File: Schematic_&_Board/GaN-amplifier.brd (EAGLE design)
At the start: 120.7 x 50.8 mm, 80 parts, among them IC1 LT3080, J1 JOHNSON_SMA_EDGE_LAUNCH_142-0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, J2 JOHNSON_SMA_EDGE_LAUNCH_142-0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, Q1 MMBT3906LT1SMD, T1 IRL3714S, T2 IRL3714S, T3 IRL3714S, T4 IRL3714S, T5 BSP89, U1 TPS7A30XX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

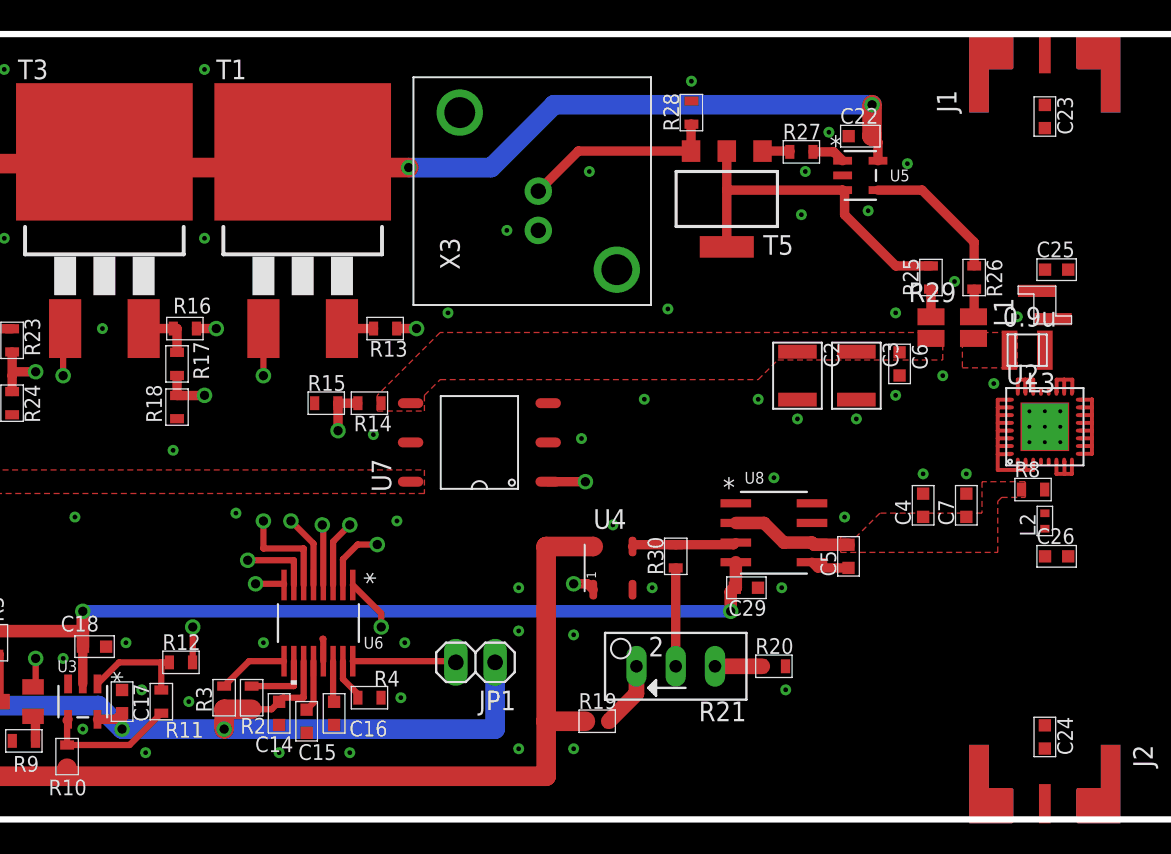
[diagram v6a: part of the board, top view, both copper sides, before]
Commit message: Finished Layout, Starting BOM
I've finished the layout up to getting final RF trace widths set (per
manufacturer specs) and started compiling a BOM.

DSB
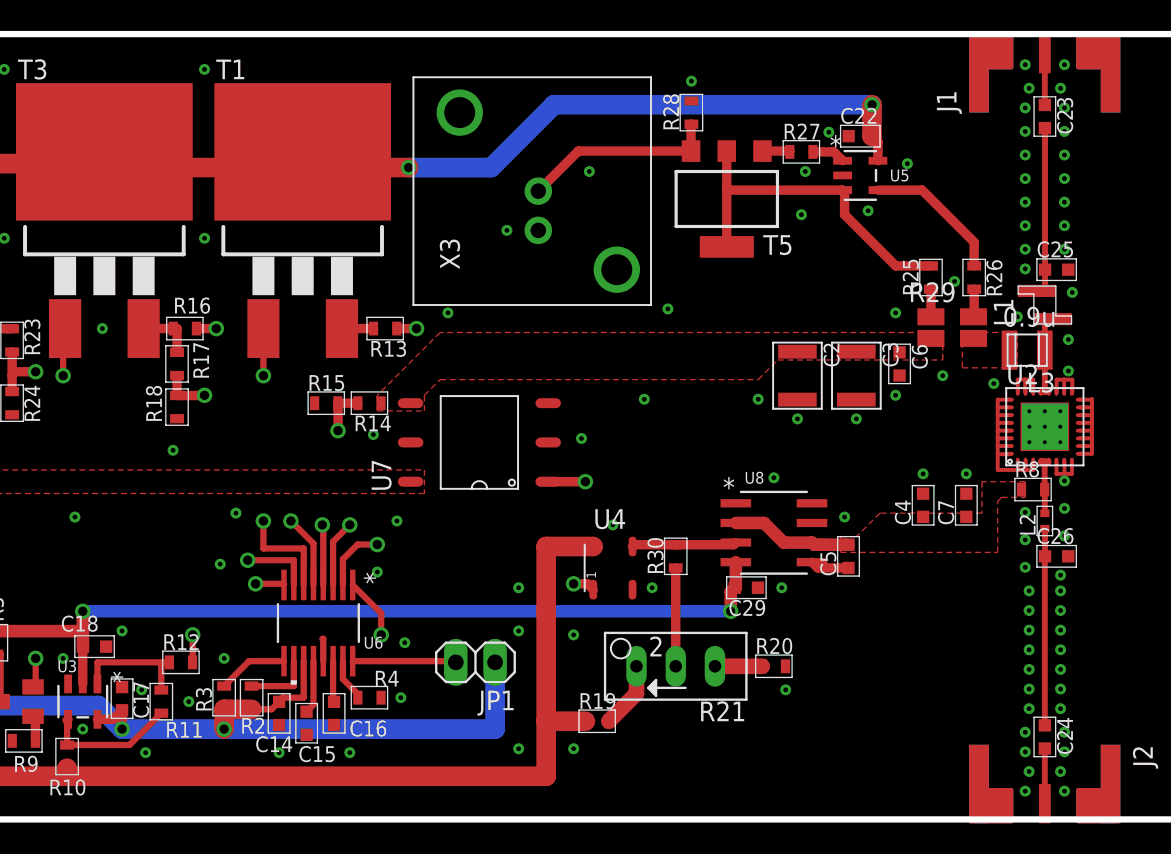
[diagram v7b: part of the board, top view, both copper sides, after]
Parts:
- R19: value 2k -> 4.02k
- R20: value 1k -> 2k
- R21: value 5k -> 10k
- R28: value 4k -> 4.02k
- T1, T2, T3, T4: value IRL3714S -> IPB080N03L G
- moved C17 0.19 mm to (45.7, 7.81)
- moved C15 0.13 mm to (57.7, 6.22)
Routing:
- net N$35: track 0.00 -> 12.7 mm
- net N$33: track 0.00 -> 11.1 mm
- net N$34: track 0.00 -> 5.97 mm
- net V_GATE: track 0.00 -> 4.10 mm
- net N$31: track 0.00 -> 3.57 mm
- net N$30: track 0.00 -> 3.31 mm
- net N$8: track 7.02 -> 7.84 mm
- net GND: vias 81 -> 134

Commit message: Finished BOM
All parts are now added to BOM.

DSB
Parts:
- C15: value 200n -> 220n
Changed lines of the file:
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@@
 <element name="C8" library="jqi_passives" package="C_MLCC_1206" value="10u" x="32.512" y="17.018" smashed="yes" rot="R90">
 <attribute name="NAME" x="34.768" y="16.088" size="1.016" layer="25" font="vector" rot="R90"/>
+<attribute name="PARTNO" value="1276-6767-1-ND" x="32.512" y="17.018" size="1.778" layer="27" rot="R90" display="off"/>
 </element>
 <element name="C9" library="jqi_passives" package="C_MLCC_1206" value="10u" x="15.24" y="15.24" smashed="yes" rot="R270">
 <attribute name="NAME" x="14.564" y="11.714" size="1.016" layer="25" font="vector"/>
+<attribute name="PARTNO" value="1276-6767-1-ND" x="15.24" y="15.24" size="1.778" layer="27" rot="R270" display="off"/>
 </element>
 <element name="C10" library="jqi_passives" package="C_MLCC_0402" value="10n" x="20.574" y="17.018" smashed="yes" rot="R180">
 <attribute name="NAME" x="21.982" y="19.212" size="1.016" layer="25" font="vector" rot="R180"/>
+<attribute name="PARTNO" value="1276-1028-1-ND" x="20.574" y="17.018" size="1.778" layer="27" rot="R180" display="off"/>
 </element>
 <element name="C11" library="jqi_passives" package="C_MLCC_0402" value="10n" x="28.702" y="16.002" smashed="yes" rot="R90">
 <attribute name="NAME" x="27.778" y="19.95" size="1.016" layer="25" font="vector" rot="R270"/>
+<attribute name="PARTNO" value="1276-1028-1-ND" x="28.702" y="16.002" size="1.778" layer="27" rot="R90" display="off"/>
 </element>
 <element name="R6" library="jqi_passives" package="R_0402" value="56k" x="29.972" y="16.002" smashed="yes" rot="R270">
@@
 <attribute name="PARTNO" value="A1921-ND" x="68.58" y="10.16" size="1.778" layer="27" rot="R180" display="off"/>
 </element>
-<element name="C15" library="jqi_passives" package="C_MLCC_0603" value="200n" x="57.658" y="6.223" smashed="yes" rot="R270">
+<element name="C15" library="jqi_passives" package="C_MLCC_0603" value="220n" x="57.658" y="6.223" smashed="yes" rot="R270">
 <attribute name="NAME" x="57.12" y="3.721" size="1.016" layer="25" font="vector"/>
+<attribute name="PARTNO" value="1276-2014-1-ND" x="57.658" y="6.223" size="1.778" layer="27" rot="R270" display="off"/>
 </element>
 <element name="C16" library="jqi_passives" package="C_MLCC_0603" value="150n" x="59.436" y="6.858" smashed="yes" rot="R270">
 <attribute name="NAME" x="60.422" y="5.372" size="1.016" layer="25" font="vector"/>
+<attribute name="PARTNO" value="1276-1973-1-ND" x="59.436" y="6.858" size="1.778" layer="27" rot="R270" display="off"/>
 </element>
 <element name="R4" library="jqi_passives" package="R_0603" value="49.9k" x="61.722" y="7.874" smashed="yes" rot="R180">
@@
 <element name="Q1" library="transistor-pnp" package="SOT23-BEC" value="MMBT3906LT1SMD" x="38.862" y="7.62" smashed="yes" rot="R90">
 <attribute name="NAME" x="36.957" y="8.509" size="1.27" layer="25" rot="R180"/>
+<attribute name="PARTNO" value="MMBT3906LT1GOSCT-ND" x="38.862" y="7.62" size="1.778" layer="27" rot="R90" display="off"/>
 </element>
 <element name="R5" library="jqi_passives" package="R_0603" value="1M" x="37.592" y="11.43" smashed="yes" rot="R90">
@@
 <attribute name="PARTNO" value="804-1093-ND" x="81.534" y="9.906" size="1.778" layer="27" rot="R180" display="off"/>
 </element>
-<element name="J1" library="connector-jqi" package="JOHNSON_SMA_EDGE_LAUNCH_142-0701-851" value="JOHNSON_SMA_EDGE_LAUNCH_142-0701-851" x="105.41" y="50.8" rot="R90"/>
-<element name="J2" library="connector-jqi" package="JOHNSON_SMA_EDGE_LAUNCH_142-0701-851" value="JOHNSON_SMA_EDGE_LAUNCH_142-0701-851" x="105.41" y="-0.254" rot="R270"/>
+<element name="J1" library="connector-jqi" package="JOHNSON_SMA_EDGE_LAUNCH_142-0701-851" value="JOHNSON_SMA_EDGE_LAUNCH_142-0701-851" x="105.41" y="50.8" rot="R90">
+<attribute name="PARTNO" value="J658-ND" x="105.41" y="50.8" size="1.778" layer="27" rot="R90" display="off"/>
+</element>
+<element name="J2" library="connector-jqi" package="JOHNSON_SMA_EDGE_LAUNCH_142-0701-851" value="JOHNSON_SMA_EDGE_LAUNCH_142-0701-851" x="105.41" y="-0.254" rot="R270">
+<attribute name="PARTNO" value="J658-ND" x="105.41" y="-0.254" size="1.778" layer="27" rot="R270" display="off"/>
+</element>
 <element name="U8" library="linear-technology-jqi" package="SO-8_S" value="LTC1152IS8TRPBF" x="87.884" y="18.542">
 <attribute name="VENDOR" value="Linear Technology" x="87.884" y="18.542" size="1.778" layer="27" display="off"/>
@@
 <attribute name="PARTNO" value="LTC1152IS8#PBF-ND" x="87.884" y="18.542" size="1.778" layer="27" display="off"/>
 </element>
-<element name="C4" library="jqi_passives" package="C_MLCC_0603" value="1u" x="97.536" y="20.32" rot="R90"/>
-<element name="C5" library="jqi_passives" package="C_MLCC_0603" value="1n" x="92.71" y="17.018" rot="R90"/>
+<element name="C4" library="jqi_passives" package="C_MLCC_0603" value="1u" x="97.536" y="20.32" rot="R90">
+<attribute name="PARTNO" value="1276-1184-1-ND" x="97.536" y="20.32" size="1.778" layer="27" rot="R90" display="off"/>
+</element>
+<element name="C5" library="jqi_passives" package="C_MLCC_0603" value="1n" x="92.71" y="17.018" rot="R90">
+<attribute name="PARTNO" value="1276-1195-1-ND" x="92.71" y="17.018" size="1.778" layer="27" rot="R90" display="off"/>
+</element>
 <element name="R30" library="jqi_passives" package="R_0603" value="50" x="81.534" y="17.018" rot="R90">
 <attribute name="PARTNO" value="P49.9HCT-ND" x="81.534" y="17.018" size="1.778" layer="27" rot="R90" display="off"/>
